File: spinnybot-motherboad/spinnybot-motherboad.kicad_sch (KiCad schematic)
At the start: 48 parts, among them J1 +12V, J11 CAP SWITCH, J12 LEDSTRIP3, J13 LEDSTRIP2, J14 LEDSTRIP3, J2 LEDSTRIP1, J3 LEDSTRIP1, J4 LEDSTRIP2, J5 GND, J6 MOTOR2, J7 MOTOR3, J8 MOTOR1, J9 CAP SWITCH, Q1 SISA96DN, Q2 SISA96DN, Q4 NPN, Q5 PNP, U1 LM1117-3.3, U2 XBP9B-DMWT-002, U3 SN74LVC1G74

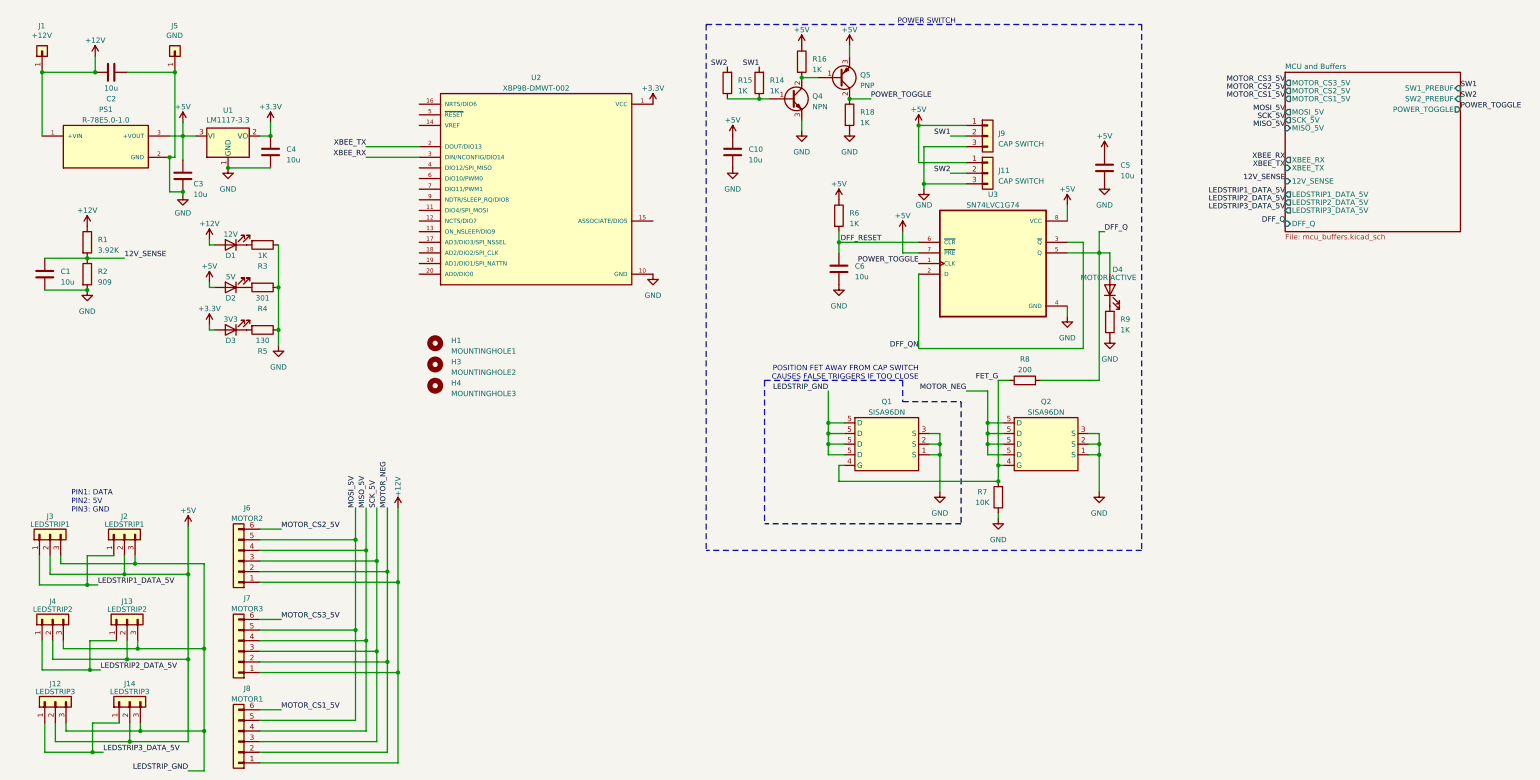
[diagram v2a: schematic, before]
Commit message: added PDF schematic and fixed a routing error
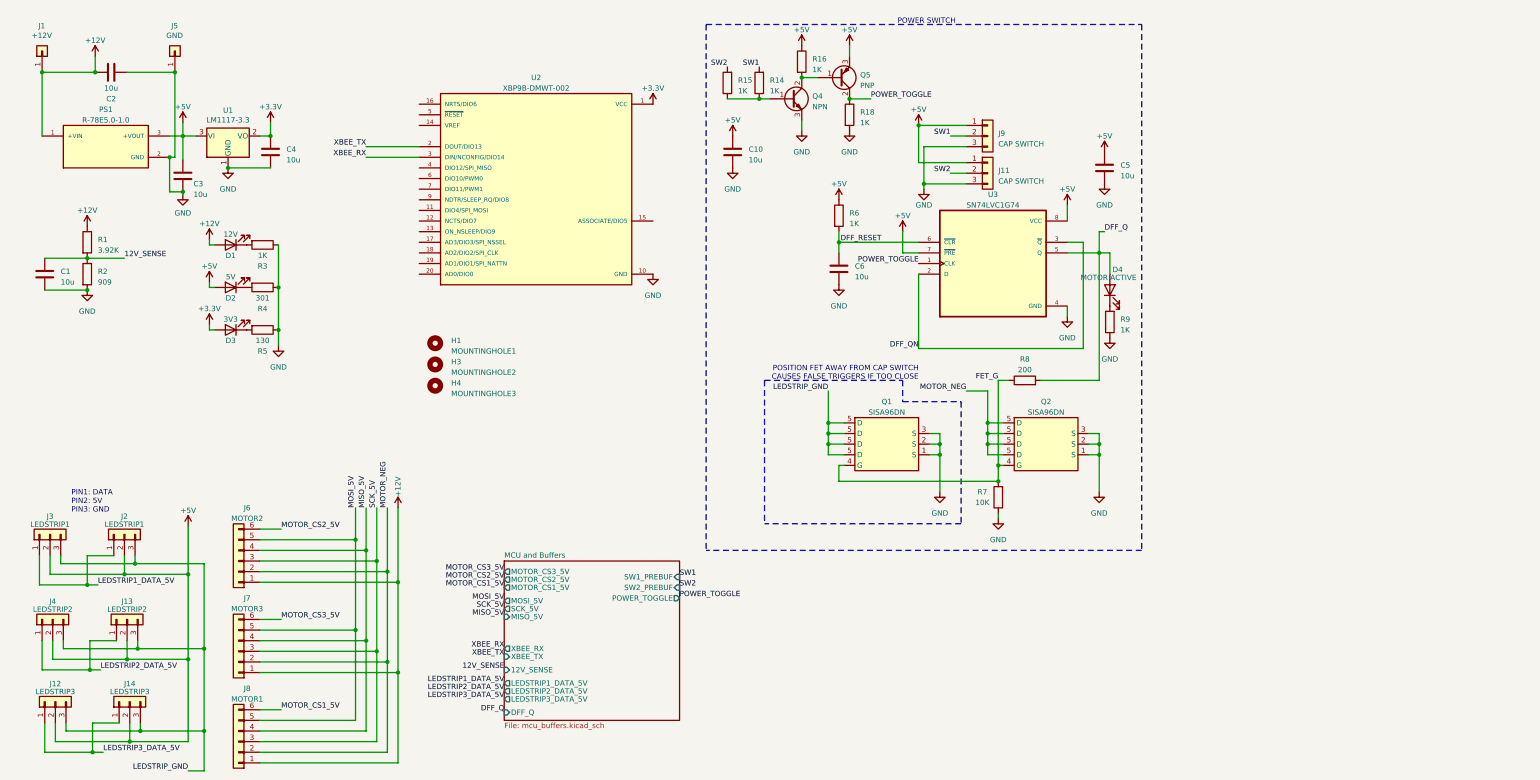
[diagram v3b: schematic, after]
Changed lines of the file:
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@@
+    (effects (font (size 1.27 1.27)) (justify left bottom))
+  )
+  (label "MOTOR_CS3_5V" (at 130.81 147.32 180)
+    (effects (font (size 1.27 1.27)) (justify right bottom))
+  )
+  (label "MOTOR_CS2_5V" (at 130.81 149.225 180)
+    (effects (font (size 1.27 1.27)) (justify right bottom))
+  )
+  (label "MOTOR_CS1_5V" (at 130.81 151.13 180)
+    (effects (font (size 1.27 1.27)) (justify right bottom))
+  )
+  (label "MOSI_5V" (at 130.81 154.305 180)
+    (effects (font (size 1.27 1.27)) (justify right bottom))
+  )
+  (label "SCK_5V" (at 130.81 156.21 180)
+    (effects (font (size 1.27 1.27)) (justify right bottom))
+  )
+  (label "MISO_5V" (at 130.81 158.115 180)
+    (effects (font (size 1.27 1.27)) (justify right bottom))
+  )
+  (label "XBEE_RX" (at 130.81 165.735 180)
+    (effects (font (size 1.27 1.27)) (justify right bottom))
+  )
+  (label "XBEE_TX" (at 130.81 167.64 180)
+    (effects (font (size 1.27 1.27)) (justify right bottom))
+  )
+  (label "12V_SENSE" (at 130.81 170.815 180)
+    (effects (font (size 1.27 1.27)) (justify right bottom))
+  )
+  (label "LEDSTRIP1_DATA_5V" (at 130.81 173.99 180)
+    (effects (font (size 1.27 1.27)) (justify right bottom))
+  )
+  (label "LEDSTRIP2_DATA_5V" (at 130.81 175.895 180)
+    (effects (font (size 1.27 1.27)) (justify right bottom))
+  )
+  (label "LEDSTRIP3_DATA_5V" (at 130.81 177.8 180)
+    (effects (font (size 1.27 1.27)) (justify right bottom))
+  )
+  (label "DFF_Q" (at 130.81 180.975 180)
+    (effects (font (size 1.27 1.27)) (justify right bottom))
+  )
+  (label "SW1" (at 172.72 148.59 0)
+    (effects (font (size 1.27 1.27)) (justify left bottom))
+  )
+  (label "SW2" (at 172.72 151.13 0)
+    (effects (font (size 1.27 1.27)) (justify left bottom))
+  )
+  (label "POWER_TOGGLE" (at 172.72 153.67 0)
     (effects (font (size 1.27 1.27)) (justify left bottom))
   )
@@
   )
   (label "DFF_Q" (at 274.32 66.04 0)
-    (effects (font (size 1.27 1.27)) (justify left bottom))
-  )
-  (label "MOTOR_CS3_5V" (at 317.5 30.48 180)
-    (effects (font (size 1.27 1.27)) (justify right bottom))
-  )
-  (label "MOTOR_CS2_5V" (at 317.5 32.385 180)
-    (effects (font (size 1.27 1.27)) (justify right bottom))
-  )
-  (label "MOTOR_CS1_5V" (at 317.5 34.29 180)
-    (effects (font (size 1.27 1.27)) (justify right bottom))
-  )
-  (label "MOSI_5V" (at 317.5 37.465 180)
-    (effects (font (size 1.27 1.27)) (justify right bottom))
-  )
-  (label "SCK_5V" (at 317.5 39.37 180)
-    (effects (font (size 1.27 1.27)) (justify right bottom))
-  )
-  (label "MISO_5V" (at 317.5 41.275 180)
-    (effects (font (size 1.27 1.27)) (justify right bottom))
-  )
-  (label "XBEE_RX" (at 317.5 48.895 180)
-    (effects (font (size 1.27 1.27)) (justify right bottom))
-  )
-  (label "XBEE_TX" (at 317.5 50.8 180)
-    (effects (font (size 1.27 1.27)) (justify right bottom))
-  )
-  (label "12V_SENSE" (at 317.5 53.975 180)
-    (effects (font (size 1.27 1.27)) (justify right bottom))
-  )
-  (label "LEDSTRIP1_DATA_5V" (at 317.5 57.15 180)
-    (effects (font (size 1.27 1.27)) (justify right bottom))
-  )
-  (label "LEDSTRIP2_DATA_5V" (at 317.5 59.055 180)
-    (effects (font (size 1.27 1.27)) (justify right bottom))
-  )
-  (label "LEDSTRIP3_DATA_5V" (at 317.5 60.96 180)
-    (effects (font (size 1.27 1.27)) (justify right bottom))
-  )
-  (label "DFF_Q" (at 317.5 64.135 180)
-    (effects (font (size 1.27 1.27)) (justify right bottom))
-  )
-  (label "SW1" (at 359.41 31.75 0)
-    (effects (font (size 1.27 1.27)) (justify left bottom))
-  )
-  (label "SW2" (at 359.41 34.29 0)
-    (effects (font (size 1.27 1.27)) (justify left bottom))
-  )
-  (label "POWER_TOGGLE" (at 359.41 36.83 0)
     (effects (font (size 1.27 1.27)) (justify left bottom))
   )
@@
     (pin "9")
   )
-  (sheet (at 317.5 27.94) (size 41.91 38.1) (fields_autoplaced)
+  (sheet (at 130.81 144.78) (size 41.91 38.1) (fields_autoplaced)
     (stroke (width 0.0006) (type solid) (color 0 0 0 0))
     (fill (color 0 0 0 0.0000))
-    (property "Sheet name" "MCU and Buffers" (id 0) (at 317.5 27.3043 0)
+    (property "Sheet name" "MCU and Buffers" (id 0) (at 130.81 144.1443 0)
       (effects (font (size 1.27 1.27)) (justify left bottom))
     )
-    (property "Sheet file" "mcu_buffers.kicad_sch" (id 1) (at 317.5 66.5487 0)
+    (property "Sheet file" "mcu_buffers.kicad_sch" (id 1) (at 130.81 183.3887 0)
       (effects (font (size 1.27 1.27)) (justify left top))
     )
-    (pin "MOTOR_CS3_5V" output (at 317.5 30.48 180)
-      (effects (font (size 1.27 1.27)) (justify left))
-    )
-    (pin "MOTOR_CS2_5V" output (at 317.5 32.385 180)
-      (effects (font (size 1.27 1.27)) (justify left))
-    )
-    (pin "MOTOR_CS1_5V" output (at 317.5 34.29 180)
-      (effects (font (size 1.27 1.27)) (justify left))
-    )
-    (pin "MOSI_5V" output (at 317.5 37.465 180)
-      (effects (font (size 1.27 1.27)) (justify left))
-    )
-    (pin "SCK_5V" output (at 317.5 39.37 180)
-      (effects (font (size 1.27 1.27)) (justify left))
-    )
-    (pin "XBEE_RX" output (at 317.5 48.895 180)
-      (effects (font (size 1.27 1.27)) (justify left))
-    )
-    (pin "XBEE_TX" input (at 317.5 50.8 180)
-      (effects (font (size 1.27 1.27)) (justify left))
-    )
-    (pin "12V_SENSE" input (at 317.5 53.975 180)
-      (effects (font (size 1.27 1.27)) (justify left))
-    )
-    (pin "LEDSTRIP1_DATA_5V" output (at 317.5 57.15 180)
-      (effects (font (size 1.27 1.27)) (justify left))
-    )
-    (pin "LEDSTRIP2_DATA_5V" output (at 317.5 59.055 180)
-      (effects (font (size 1.27 1.27)) (justify left))
-    )
-    (pin "LEDSTRIP3_DATA_5V" output (at 317.5 60.96 180)
-      (effects (font (size 1.27 1.27)) (justify left))
-    )
-    (pin "DFF_Q" input (at 317.5 64.135 180)
-      (effects (font (size 1.27 1.27)) (justify left))
-    )
-    (pin "MISO_5V" input (at 317.5 41.275 180)
-      (effects (font (size 1.27 1.27)) (justify left))
-    )
-    (pin "POWER_TOGGLE" output (at 359.41 36.83 0)
-      (effects (font (size 1.27 1.27)) (justify right))
-    )
-    (pin "SW1_PREBUF" input (at 359.41 31.75 0)
-      (effects (font (size 1.27 1.27)) (justify right))
-    )
-    (pin "SW2_PREBUF" input (at 359.41 34.29 0)
-      (effects (font (size 1.27 1.27)) (justify right))
-    )
+    (pin "MOTOR_CS3_5V" output (at 130.81 147.32 180)
+      (effects (font (size 1.27 1.27)) (justify left))
+    )
+    (pin "MOTOR_CS2_5V" output (at 130.81 149.225 180)
+      (effects (font (size 1.27 1.27)) (justify left))
+    )
+    (pin "MOTOR_CS1_5V" output (at 130.81 151.13 180)
+      (effects (font (size 1.27 1.27)) (justify left))
+    )
+    (pin "MOSI_5V" output (at 130.81 154.305 180)
+      (effects (font (size 1.27 1.27)) (justify left))
+    )
+    (pin "SCK_5V" output (at 130.81 156.21 180)
+      (effects (font (size 1.27 1.27)) (justify left))
+    )
+    (pin "XBEE_RX" output (at 130.81 165.735 180)
+      (effects (font (size 1.27 1.27)) (justify left))
+    )
+    (pin "XBEE_TX" input (at 130.81 167.64 180)
+      (effects (font (size 1.27 1.27)) (justify left))
+    )
+    (pin "12V_SENSE" input (at 130.81 170.815 180)
+      (effects (font (size 1.27 1.27)) (justify left))
+    )
+    (pin "LEDSTRIP1_DATA_5V" output (at 130.81 173.99 180)
+      (effects (font (size 1.27 1.27)) (justify left))
+    )
+    (pin "LEDSTRIP2_DATA_5V" output (at 130.81 175.895 180)
+      (effects (font (size 1.27 1.27)) (justify left))
+    )
+    (pin "LEDSTRIP3_DATA_5V" output (at 130.81 177.8 180)
+      (effects (font (size 1.27 1.27)) (justify left))
+    )
+    (pin "DFF_Q" input (at 130.81 180.975 180)
+      (effects (font (size 1.27 1.27)) (justify left))
+    )
+    (pin "MISO_5V" input (at 130.81 158.115 180)
+      (effects (font (size 1.27 1.27)) (justify left))
+    )
+    (pin "POWER_TOGGLE" output (at 172.72 153.67 0)
+      (effects (font (size 1.27 1.27)) (justify right))
+    )
+    (pin "SW1_PREBUF" input (at 172.72 148.59 0)
+      (effects (font (size 1.27 1.27)) (justify right))
+    )
+    (pin "SW2_PREBUF" input (at 172.72 151.13 0)
+      (effects (font (size 1.27 1.27)) (justify right))
+    )

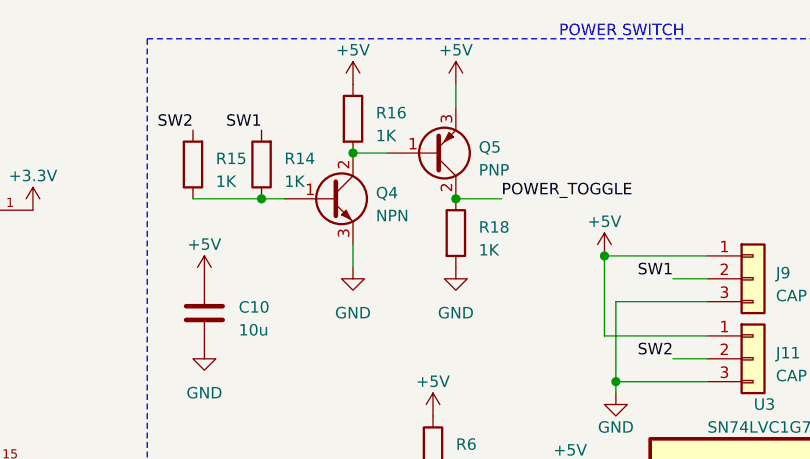
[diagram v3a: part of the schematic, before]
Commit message: Replaced transistor symbols and footprints with correct ones.
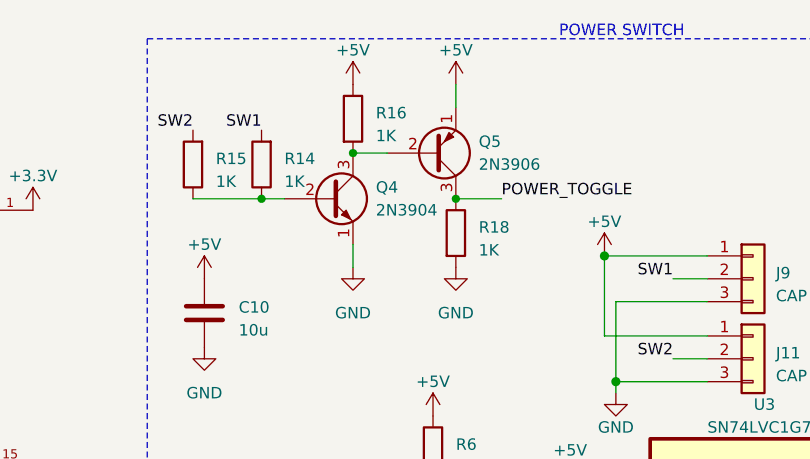
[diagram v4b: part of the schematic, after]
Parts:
- removed Q4: NPN, Package_TO_SOT_THT:TO-92_Inline, symbol Device:Q_NPN_BCE
- removed Q5: PNP, Package_TO_SOT_THT:TO-92_Inline, symbol Device:Q_PNP_BCE
- added Q4: 2N3904, Package_TO_SOT_THT:TO-92_Inline, symbol Transistor_BJT:2N3904
- added Q5: 2N3906, Package_TO_SOT_THT:TO-92_Inline, symbol Transistor_BJT:2N3906
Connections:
- net +5V: now also Q5.1 (E)
- net GND: now also Q4.1 (E)
- net POWER_TOGGLE: now also Q5.3 (C)
- net at R14.1, R15.1: now also Q4.2 (B)
- net at R16.2: now also Q4.3 (C), Q5.2 (B)
